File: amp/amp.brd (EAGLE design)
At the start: 99.1 x 80 mm, 73 parts, among them IC1 OPA2134PA, Q1 BC547, Q10 IRF540, Q11 BC556, Q12 BC556, Q13 BC547, Q14 BC547, Q15 2N7000, Q16 BC337, Q17 BC337, Q18 IRF540, Q19 IRF540, Q2 BC556, Q20 BC547, Q3 BC547, Q4 BC556, Q5 2N7000, Q6 BC337, Q7 BC337, Q8 BC547, Q9 IRF540

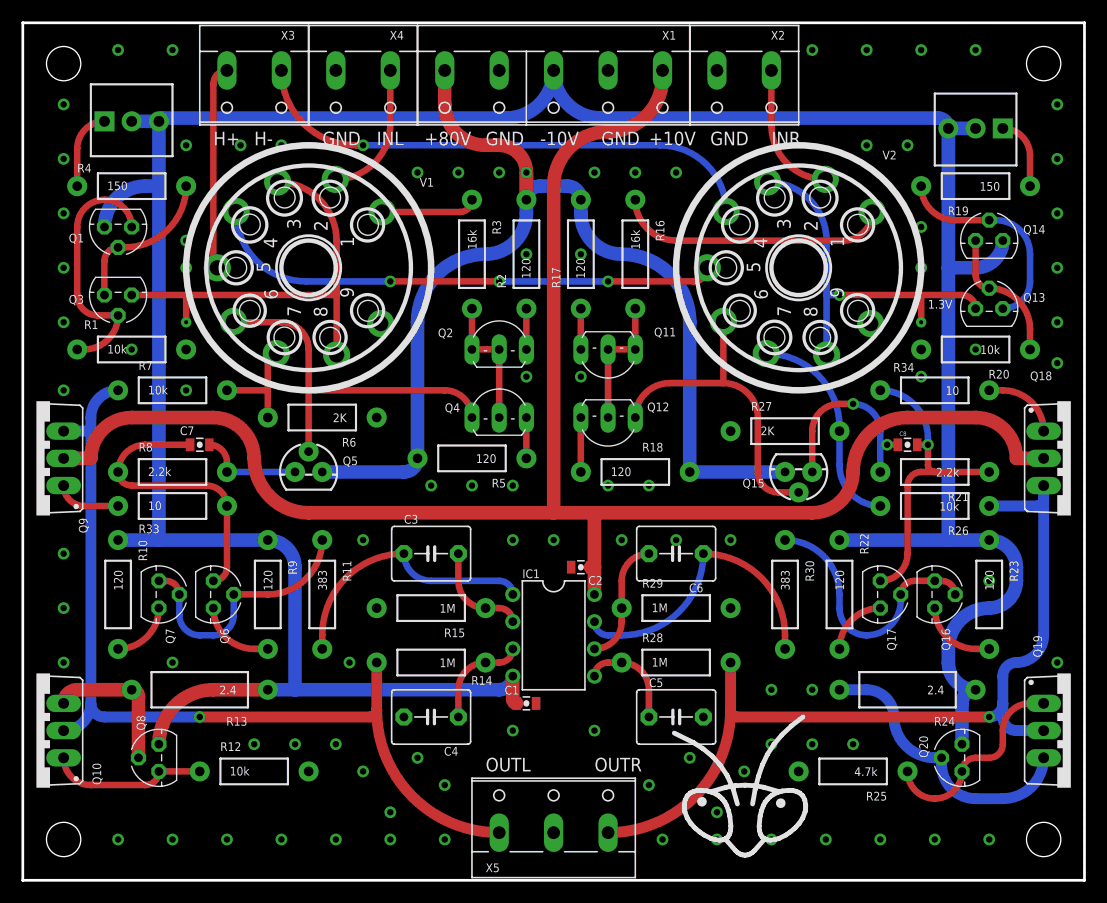
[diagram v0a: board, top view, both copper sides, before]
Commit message: High frequency snubber
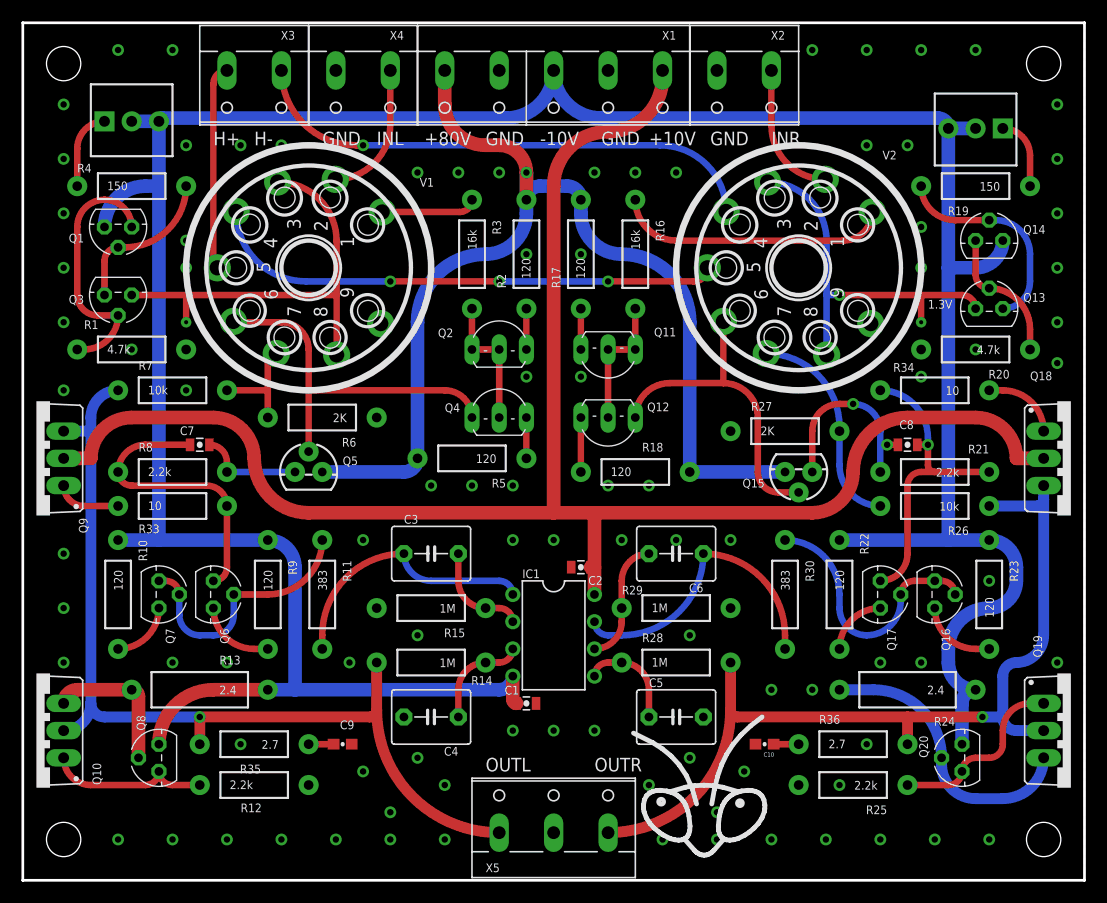
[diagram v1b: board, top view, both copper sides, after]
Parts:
- added C10, C9: 0.1uF, SparkFun-Capacitors:0603-CAP
- added R35, R36: 2.7, SparkFun-Resistors:AXIAL-0.4
- R1, R20: value 10k -> 4.7k
- R12: value 10k -> 2.2k
- R25: value 4.7k -> 2.2k
- moved LOGO1 3.81 mm to (63.5, 8.89)
- moved R12 1.27 mm to (21.6, 8.89)
- moved R25 1.27 mm to (77.5, 8.89)
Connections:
- new net N$43: C9.1, R35.P$1
- new net N$44: C10.1, R36.P$1
- net GND: now also C10.2, C9.2
- net OUTL: now also R35.P$2
- net OUTR: now also R36.P$2
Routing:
- net OUTL: track 84.5 -> 87.0 mm
- net N$44: track 0.00 -> 2.33 mm
- net N$43: track 0.00 -> 2.32 mm
- net OUTR: track 79.6 -> 81.7 mm
- net N$33: track 18.2 -> 16.6 mm
- net N$15: track 14.3 -> 14.8 mm

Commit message: MOSFET driver stage
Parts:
- removed C10, C9: 0.1uF, SparkFun-Capacitors:0603-CAP
- removed C7, C8: 82nF, SparkFun-Capacitors:0805-CAP
- added Q21, Q22: BC547, transistor-npn:TO92
- added Q23, Q24: IRF540, transistor-power:TO220BV
- Q10, Q18, Q19, Q9: value IRF540 -> BC547; device transistor-power:TO220BV -> transistor-npn:TO92
- Q11, Q12: value BC556 -> IRF540; device my:TO92-BENT -> transistor-power:TO220BV
- Q14: value BC547 -> BC556; device transistor-npn:TO92 -> my:TO92-BENT
- Q15: value 2N7000 -> BC547; device SparkFun-DiscreteSemi:TO-92 -> transistor-npn:TO92
- Q16: value BC337 -> BC556; device transistor:TO92 -> my:TO92-BENT
- Q17: value BC337 -> 2N7000; device transistor:TO92 -> SparkFun-DiscreteSemi:TO-92
- Q6, Q7: value BC337 -> BC547; device transistor:TO92 -> transistor-npn:TO92
- R11, R30: value 383 -> 120
- R12: value 2.2k -> 120
- R13: value 2.4 -> 549; device SparkFun-Resistors:AXIAL-0.5 -> SparkFun-Resistors:AXIAL-0.4
- R14: value 1M -> 220
- R15: value 1M -> 2.2k
- R16: value 16k -> 2.4; device SparkFun-Resistors:AXIAL-0.4 -> SparkFun-Resistors:AXIAL-0.5
- R17, R18: value 120 -> 1M
- R19: value 150 -> 4.7k
- R20: value 4.7k -> 120
- R21: value 2.2k -> 16k
- R22: value 120 -> 150
- R23, R5: value 120 -> 500; device SparkFun-Resistors:AXIAL-0.4 -> SparkFun-Electromechanical:3362U-2
- R24: value 2.4 -> 120; device SparkFun-Resistors:AXIAL-0.5 -> SparkFun-Resistors:AXIAL-0.4
- R25: value 2.2k -> 2K
- R27: value 2K -> 2.61k
- R28, R29: value 1M -> 120
- R31: value 500 -> 549; device SparkFun-Electromechanical:3362U-2 -> SparkFun-Resistors:AXIAL-0.4
- R32: value 500 -> 220; device SparkFun-Electromechanical:3362U-2 -> SparkFun-Resistors:AXIAL-0.4
- R33: value 10 -> 2.2k
- R34: value 10 -> 2.4; device SparkFun-Resistors:AXIAL-0.4 -> SparkFun-Resistors:AXIAL-0.5
- R35, R36: value 2.7 -> 1M
- R6: value 2K -> 120
- R7: value 10k -> 2K
- R8: value 2.2k -> 10k
- R9: value 120 -> 2.61k
- moved R31 81.3 mm to (73.7, 20.3), turned to 180 degrees
- moved R33 76.5 mm to (86.4, 10.2), turned to 180 degrees
- moved Q12 60.2 mm to (1.27, 14.0), turned to 90 degrees
- moved R16 54.4 mm to (24.1, 15.2), turned to 180 degrees
- moved Q11 54.1 mm to (1.27, 39.4), turned to 90 degrees
- moved R5 44.9 mm to (10.2, 71.1), turned to 0 degrees
- moved R23 43.2 mm to (88.9, 69.8), turned to 180 degrees
- moved R17 40.6 mm to (38.1, 20.3), turned to 180 degrees
- moved R22 40.2 mm to (88.9, 64.8), turned to 180 degrees
- moved R35 40.1 mm to (61.0, 20.3), turned to 0 degrees
- moved R20 37.9 mm to (52.1, 58.4), turned to 90 degrees
- moved Q14 37.4 mm to (54.6, 48.3), turned to 180 degrees
- moved R32 36.9 mm to (86.4, 33.0)
- moved LOGO1 35.6 mm to (27.9, 8.89)
- moved R21 34.5 mm to (57.1, 58.4), turned to 270 degrees
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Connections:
- new net N$45: Q7.1, Q8.3, R14.P$2
- new net N$46: Q20.1, R29.P$2
- net GND: now also C6.2, R18.P$2, R19.P$2, R25.P$1, R33.P$2, R36.P$2, R7.P$1, X3.2; no longer C10.2, C5.2, C9.2, R12.P$2, R20.P$2, R25.P$2, R27.P$1, R29.P$2, R6.P$1, X4.2
- net HIN: now also X4.2; no longer X3.2
- net HOUT: now also X4.1; no longer X3.1
- net HT: now also Q17.3, R20.P$2, R24.P$2, R6.P$2; no longer Q15.3, R17.P$2, R18.P$2, R5.P$2
- net INL: now also X3.1; no longer X4.1
- net N$10: now also Q8.2, Q9.2, Q9.3, R13.P$1; no longer Q7.2, Q7.3, R11.P$1
- net N$11: now also R10.P$2; no longer R9.P$2
- net N$12: now also Q9.1, R12.P$2; no longer Q7.1, R10.P$2
- net N$13: now also Q18.3, Q19.2, R27.P$1; no longer C7.2, Q6.3, R33.P$2, R8.P$1
- net N$14: now also R9.P$2; no longer C7.1, R8.P$2
- net N$15: now also Q10.3, Q12.G, R15.P$1; no longer Q10.G, Q8.3, R12.P$1
- net N$16: now also Q10.2, Q12.S, R16.P$2; no longer Q10.S, Q8.2, R13.P$2
- net N$17: now also R18.P$1; no longer R15.P$1
- net N$18: now also Q15.3; no longer Q13.3
- net N$19: now also R17.P$1; no longer R14.P$1
- net N$20: now also Q14.1, Q14.2, Q16.2, R21.P$2; no longer Q11.1, Q11.2, Q12.2, R16.P$2
- net N$21: now also R13.P$2; no longer R11.P$2
- net N$22: now also Q16.1, Q17.2; no longer Q12.1, Q15.2
- net N$23: now also R21.P$1; no longer R16.P$1
- net N$24: now also Q14.3, R20.P$1; no longer Q11.3, R17.P$1
- net N$25: now also Q16.3, R24.P$1; no longer Q12.3, R18.P$1
- net N$26: now also Q13.2, Q15.1, R22.P$2; no longer Q13.1, Q14.2, R19.P$2
- net N$27: now also Q13.3, Q15.2, R19.P$1; no longer Q13.2, Q14.3, R20.P$1
- net N$28: now also Q18.2, Q20.2, Q21.2, Q21.3, R31.P$1; no longer Q16.2, Q16.3, Q17.2, R30.P$1
- net N$29: now also Q18.1, R28.P$2; no longer Q17.1, R22.P$2
- net N$30: now also Q21.1, R30.P$2; no longer Q16.1, R23.P$2
- net N$31: now also Q19.1, Q20.3, R32.P$2; no longer C8.2, Q17.3, R21.P$1, R34.P$2
- net N$32: now also Q8.1, R11.P$2; no longer C8.1, Q15.1, R21.P$2
- net N$33: now also Q22.3, Q24.G, R33.P$1; no longer Q19.G, Q20.3, R25.P$1
- net N$34: now also Q22.2, Q24.S, R34.P$2; no longer Q19.S, Q20.2, R24.P$2
- net N$35: now also R25.P$2; no longer R27.P$2
- net N$36: now also C5.2, R36.P$1; no longer C6.2, R29.P$1
- net N$37: now also C6.1, R35.P$1; no longer C5.1, R28.P$1
- net N$38: now also C5.1, R31.P$2; no longer C6.1, R30.P$2
- net N$39: now also R5.1; no longer R31.1
- net N$40: now also R22.P$1, R23.1; no longer R19.P$1, R32.1
- net N$41: now also Q11.G, R14.P$1; no longer Q9.G, R33.P$1
- net N$42: now also Q23.G, R32.P$1; no longer Q18.G, R34.P$1
- net N$43: now also Q17.1, R27.P$2; no longer C9.1, R35.P$1
- net N$44: now also Q6.3, Q7.2, R9.P$1; no longer C10.1, R36.P$1
- net N$6: now also R6.P$1; no longer R5.P$1
- net N$9: now also R8.P$2; no longer R6.P$2
- net OUTL: now also Q11.S, Q12.D, R17.P$2, R8.P$1; no longer Q10.D, Q9.S, R14.P$2, R35.P$2, R7.P$1
- net OUTR: now also Q23.S, Q24.D, R35.P$2; no longer Q18.S, Q19.D, R28.P$2, R36.P$2
- net VCC: now also Q11.D, Q19.3, Q23.D, Q7.3; no longer Q18.D, Q9.D
- net VEE: now also Q10.1, Q13.1, Q22.1, R11.P$1, R12.P$1, R16.P$1, R23.2, R23.3, R28.P$1, R29.P$1, R30.P$1, R34.P$1, R5.2, R5.3; no longer Q14.1, Q20.1, Q8.1, R13.P$1, R22.P$1, R23.P$1, R24.P$1, R31.2, R31.3, R32.2, R32.3, R9.P$1
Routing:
- net N$45: track 0.00 -> 17.1 mm, vias 0 -> 1
- net N$44: track 2.33 -> 19.4 mm, vias 0 -> 1
- net N$11: track 6.66 -> 23.6 mm, vias 0 -> 1
- net N$46: track 0.00 -> 12.3 mm
- net N$32: track 17.7 -> 6.13 mm, vias 2 -> 0
- net N$29: track 5.39 -> 16.8 mm, vias 0 -> 1
- net N$43: track 2.32 -> 11.6 mm
- net VEE: track 278.8 -> 287.8 mm
- net N$13: track 26.8 -> 18.8 mm, vias 0 -> 1
- net N$31: track 28.8 -> 21.8 mm
- net N$10: track 23.3 -> 29.5 mm
- net N$28: track 23.3 -> 29.5 mm
- net N$42: track 6.66 -> 11.9 mm, vias 0 -> 1
- net N$34: track 25.2 -> 20.6 mm
- net N$38: track 25.9 -> 21.4 mm
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
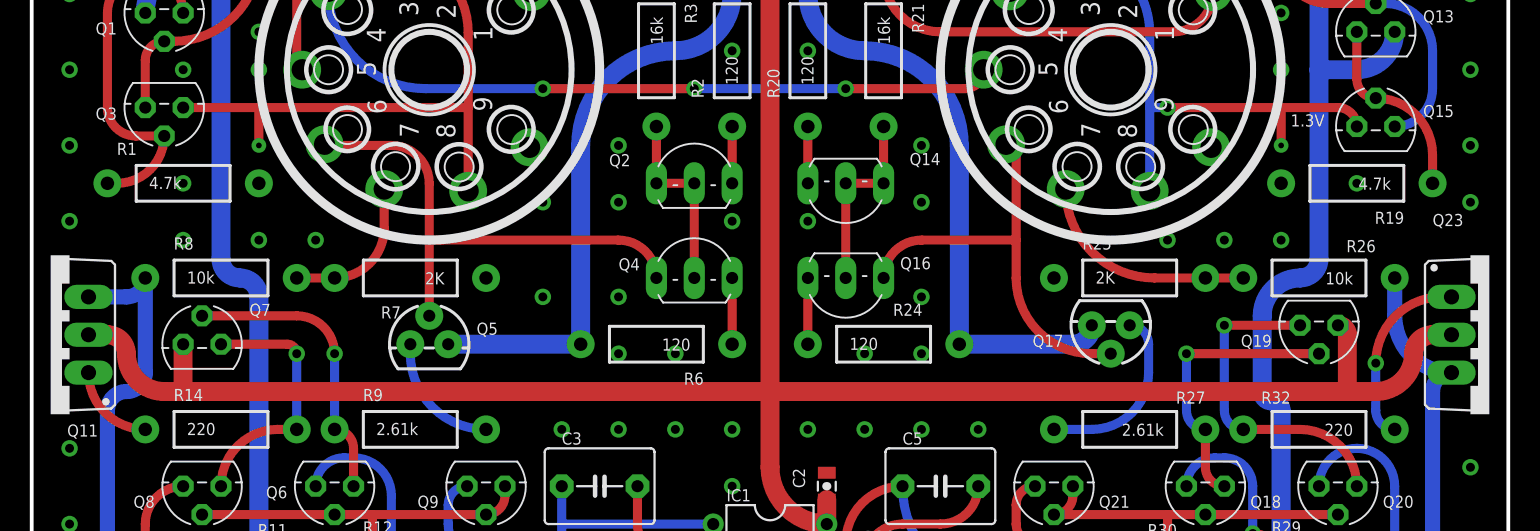
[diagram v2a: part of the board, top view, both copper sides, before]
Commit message: Gain switching jumper
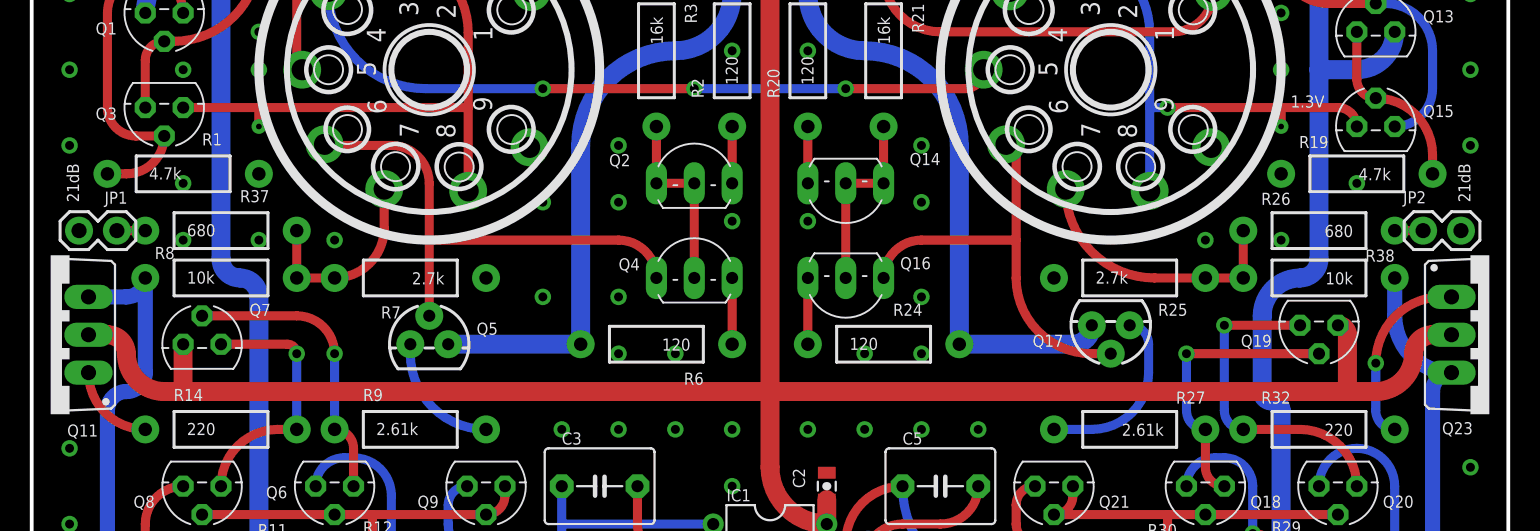
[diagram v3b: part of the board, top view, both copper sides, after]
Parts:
- added JP1, JP2: (no value), SparkFun-Retired:1X02
- added R37, R38: 680, SparkFun-Resistors:AXIAL-0.4
- R25, R7: value 2K -> 2.7k
- moved TP1 1.27 mm to (83.8, 53.3)
- moved TP2 1.27 mm to (15.2, 53.3)
- moved R1 0.63 mm to (10.2, 50.2)
- moved R19 0.63 mm to (88.9, 50.2)
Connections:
- new net N$47: JP1.1, R37.P$1
- new net N$48: JP2.1, R38.P$1
- net GND: now also JP1.2, JP2.2
- net N$35: now also R38.P$2
- net N$9: now also R37.P$2
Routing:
- net N$9: track 9.89 -> 13.1 mm
- net N$35: track 14.4 -> 17.6 mm
- net N$48: track 0.00 -> 1.91 mm
- net N$47: track 0.00 -> 1.91 mm
- net N$18: track 35.4 -> 34.1 mm
- net N$1: track 40.1 -> 38.8 mm
- net N$27: track 12.3 -> 11.6 mm
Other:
- board text added: "21dB"

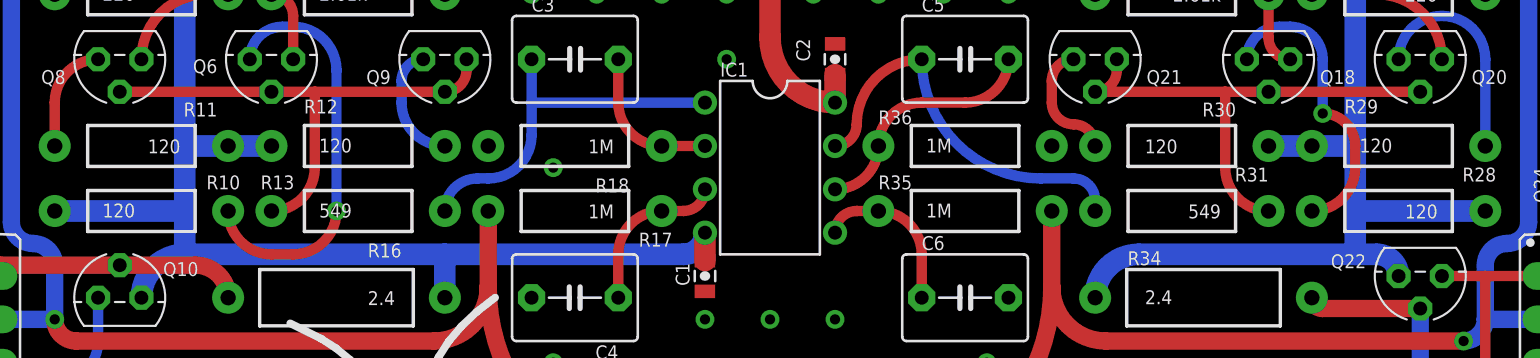
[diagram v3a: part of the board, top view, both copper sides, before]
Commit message: CM degeneration values lowered
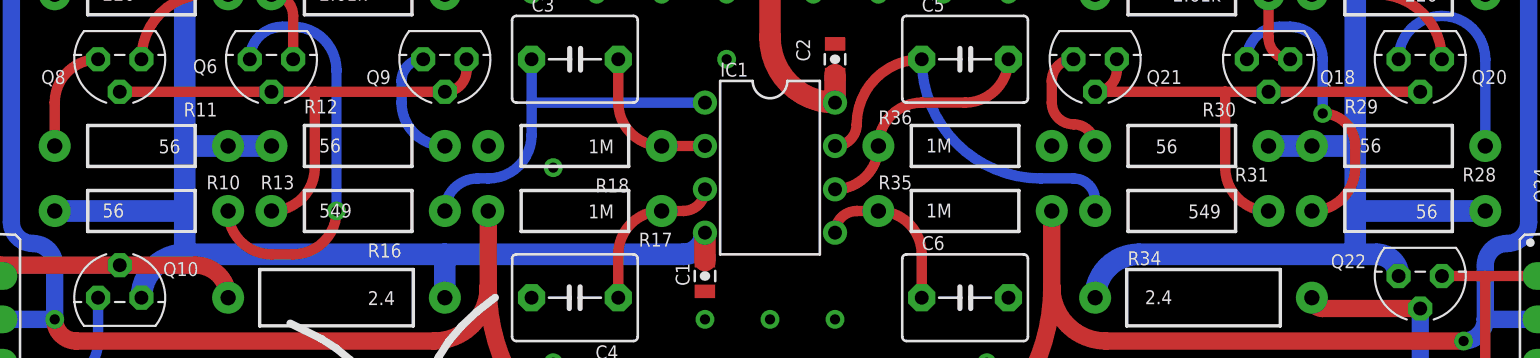
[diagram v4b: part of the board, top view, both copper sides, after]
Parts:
- R10, R11, R12, R28, R29, R30: value 120 -> 56
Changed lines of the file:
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@@
 <?xml version="1.0" encoding="utf-8"?>
 <!DOCTYPE eagle SYSTEM "eagle.dtd">
-<eagle version="7.6.0">
+<eagle version="7.7.0">
 <drawing>
 <settings>
@@
 <attribute name="VALUE" x="17.78" y="31.115" size="0.8128" layer="27" ratio="15" rot="R180"/>
 </element>
-<element name="R10" library="SparkFun-Resistors" package="AXIAL-0.4" value="120" x="12.7" y="20.32" smashed="yes">
+<element name="R10" library="SparkFun-Resistors" package="AXIAL-0.4" value="56" x="12.7" y="20.32" smashed="yes">
 <attribute name="NAME" x="16.51" y="21.59" size="0.8128" layer="25" font="vector" ratio="15"/>
 <attribute name="VALUE" x="10.414" y="19.939" size="0.8128" layer="21" font="vector" ratio="15"/>
 </element>
-<element name="R12" library="SparkFun-Resistors" package="AXIAL-0.4" value="120" x="25.4" y="24.13" smashed="yes">
+<element name="R12" library="SparkFun-Resistors" package="AXIAL-0.4" value="56" x="25.4" y="24.13" smashed="yes">
 <attribute name="NAME" x="22.225" y="26.035" size="0.8128" layer="25" font="vector" ratio="15"/>
 <attribute name="VALUE" x="23.114" y="23.749" size="0.8128" layer="21" font="vector" ratio="15"/>
@@
 <attribute name="VALUE" x="85.09" y="31.115" size="0.8128" layer="27" ratio="15" rot="R180"/>
 </element>
-<element name="R28" library="SparkFun-Resistors" package="AXIAL-0.4" value="120" x="86.36" y="20.32" smashed="yes" rot="R180">
+<element name="R28" library="SparkFun-Resistors" package="AXIAL-0.4" value="56" x="86.36" y="20.32" smashed="yes" rot="R180">
 <attribute name="NAME" x="92.075" y="22.86" size="0.8128" layer="25" font="vector" ratio="15" rot="R180"/>
 <attribute name="VALUE" x="88.646" y="20.701" size="0.8128" layer="21" font="vector" ratio="15" rot="R180"/>
 </element>
-<element name="R30" library="SparkFun-Resistors" package="AXIAL-0.4" value="120" x="73.66" y="24.13" smashed="yes" rot="R180">
+<element name="R30" library="SparkFun-Resistors" package="AXIAL-0.4" value="56" x="73.66" y="24.13" smashed="yes" rot="R180">
 <attribute name="NAME" x="76.835" y="26.67" size="0.8128" layer="25" font="vector" ratio="15" rot="R180"/>
 <attribute name="VALUE" x="73.406" y="24.511" size="0.8128" layer="21" font="vector" ratio="15" rot="R180"/>
@@
 <attribute name="VALUE" x="8.255" y="30.48" size="0.8128" layer="27" ratio="15" rot="R180"/>
 </element>
-<element name="R11" library="SparkFun-Resistors" package="AXIAL-0.4" value="120" x="12.7" y="24.13" smashed="yes" rot="R180">
+<element name="R11" library="SparkFun-Resistors" package="AXIAL-0.4" value="56" x="12.7" y="24.13" smashed="yes" rot="R180">
 <attribute name="NAME" x="17.145" y="26.67" size="0.8128" layer="25" font="vector" ratio="15" rot="R180"/>
 <attribute name="VALUE" x="14.986" y="24.511" size="0.8128" layer="21" font="vector" ratio="15" rot="R180"/>
@@
 <attribute name="VALUE" x="94.615" y="31.115" size="0.8128" layer="27" ratio="15" rot="R180"/>
 </element>
-<element name="R29" library="SparkFun-Resistors" package="AXIAL-0.4" value="120" x="86.36" y="24.13" smashed="yes">
+<element name="R29" library="SparkFun-Resistors" package="AXIAL-0.4" value="56" x="86.36" y="24.13" smashed="yes">
 <attribute name="NAME" x="83.185" y="26.035" size="0.8128" layer="25" font="vector" ratio="15"/>
 <attribute name="VALUE" x="84.074" y="23.749" size="0.8128" layer="21" font="vector" ratio="15"/>
